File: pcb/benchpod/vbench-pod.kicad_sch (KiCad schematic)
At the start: 116 parts, among them J1 PZ254V-12-22P, SW1 TS-1088-AR02016, SW2 TS-1088-AR02016, U1 ICE40UP5K-SG48ITR, U10 TCAN1044VDRBRQ1, U2 W25Q64JVSSIQ, U24 SN74LVC2G66DCUR, U28 SRV05-4.TCT, U4 ESP32-C3-MINI-1-N4, U5 STM32H563ZGT6, U7 APS6404L-3SQR-ZR, U8 TPS2116DRLR, X1 SX3M48.000B10F20TNN, Y2 6pF ±10ppm SMD2016-4P Crystal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

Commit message: analog v3r2: smaller capacitor packages (same rating and dielectric)
To 0402: 3.3 nF C99 C102 C119 C226 (C26404), 8.2 pF C0G C29 C30 C50 C51
(C1579), 5.1 pF high-Q C207 C208 (C237535; the old C2297586 had 29 in stock).
To 0603: 4.7 uF C2 C3 C5 C220 (C69335), 22 uF C16 C108 C154 C157 (C2762594),
220 nF C189 (C64705), 2.2 uF X7R VCAP C218 C219 (C415535, from 1206).

Kept: C150/C153 (4.7 uF on the ~5 V charge-pump rails, DC-bias derating),
C140 (sees up to 58 V at TVS clamp), all 10 uF and the 22 uF on >5 V rails.
Footprint changes: needs a PCB update. Netlist connectivity unchanged.

Co-Authored-By: Claude Opus 5.5 <noreply@anthropic.com>
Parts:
- C16: footprint Capacitor_SMD:C_0805_2012Metric -> Capacitor_SMD:C_0603_1608Metric; LCSC C45783 -> C2762594; MFR CL21A226MAQNNNE -> CL10A226MO7JZNC
- C2, C220, C3, C5: footprint Capacitor_SMD:C_0805_2012Metric -> Capacitor_SMD:C_0603_1608Metric; LCSC C98192 -> C69335
- C218, C219: footprint Capacitor_SMD:C_1206_3216Metric -> Capacitor_SMD:C_0603_1608Metric; LCSC C50254 -> C415535
- C50, C51: footprint Capacitor_SMD:C_0603_1608Metric -> Capacitor_SMD:C_0402_1005Metric; LCSC C1685 -> C1579
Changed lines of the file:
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@@
 			)
 		)
-		(property "Footprint" "Capacitor_SMD:C_0805_2012Metric"
+		(property "Footprint" "Capacitor_SMD:C_0603_1608Metric"
 			(at 59.9948 129.54 0)
 			(hide yes)
@@
 			)
 		)
-		(property "LCSC" "C98192"
+		(property "LCSC" "C69335"
 			(at 60.96 133.35 0)
 			(hide yes)
@@
 			)
 		)
-		(property "Footprint" "Capacitor_SMD:C_0805_2012Metric"
+		(property "Footprint" "Capacitor_SMD:C_0603_1608Metric"
 			(at 244.8052 36.83 0)
 			(hide yes)
@@
 			)
 		)
-		(property "LCSC" "C98192"
+		(property "LCSC" "C69335"
 			(at 243.84 33.02 0)
 			(hide yes)
@@
 			)
 		)
-		(property "Footprint" "Capacitor_SMD:C_0805_2012Metric"
+		(property "Footprint" "Capacitor_SMD:C_0603_1608Metric"
 			(at 18.0848 162.56 0)
 			(hide yes)
@@
 			)
 		)
-		(property "LCSC" "C98192"
+		(property "LCSC" "C69335"
 			(at 19.05 158.75 0)
 			(hide yes)
@@
 			)
 		)
-		(property "Footprint" "Capacitor_SMD:C_1206_3216Metric"
+		(property "Footprint" "Capacitor_SMD:C_0603_1608Metric"
 			(at 314.6552 236.22 0)
 			(hide yes)
@@
 			)
 		)
-		(property "LCSC" "C50254"
+		(property "LCSC" "C415535"
 			(at 313.69 232.41 0)
 			(hide yes)
@@
 			)
 		)
-		(property "Footprint" "Capacitor_SMD:C_0805_2012Metric"
+		(property "Footprint" "Capacitor_SMD:C_0603_1608Metric"
 			(at 173.6852 34.29 0)
 			(hide yes)
@@
 			)
 		)
-		(property "LCSC" "C45783"
+		(property "LCSC" "C2762594"
 			(at 172.72 30.48 0)
 			(hide yes)
@@
 			)
 		)
-		(property "MFR" "CL21A226MAQNNNE"
+		(property "MFR" "CL10A226MO7JZNC"
 			(at 172.72 30.48 0)
 			(hide yes)
@@
 			)
 		)
-		(property "Footprint" "Capacitor_SMD:C_0603_1608Metric"
+		(property "Footprint" "Capacitor_SMD:C_0402_1005Metric"
 			(at 240.3348 177.8 0)
 			(hide yes)
@@
 			)
 		)
-		(property "LCSC" "C1685"
+		(property "LCSC" "C1579"
 			(at 241.3 173.99 0)
 			(hide yes)
@@
 			)
 		)
-		(property "Footprint" "Capacitor_SMD:C_1206_3216Metric"
+		(property "Footprint" "Capacitor_SMD:C_0603_1608Metric"
 			(at 392.1252 36.83 0)
 			(hide yes)
@@
 			)
 		)
-		(property "LCSC" "C50254"
+		(property "LCSC" "C415535"
 			(at 391.16 33.02 0)
 			(hide yes)
@@
 			)
 		)
-		(property "Footprint" "Capacitor_SMD:C_0603_1608Metric"
+		(property "Footprint" "Capacitor_SMD:C_0402_1005Metric"
 			(at 230.1748 170.18 0)
 			(hide yes)
@@
 			)
 		)
-		(property "LCSC" "C1685"
+		(property "LCSC" "C1579"
 			(at 231.14 166.37 0)
 			(hide yes)
@@
 			)
 		)
-		(property "Footprint" "Capacitor_SMD:C_0805_2012Metric"
+		(property "Footprint" "Capacitor_SMD:C_0603_1608Metric"
 			(at 25.7048 133.35 0)
 			(hide yes)
@@
 			)
 		)
-		(property "LCSC" "C98192"
+		(property "LCSC" "C69335"
 			(at 26.67 129.54 0)
 			(hide yes)

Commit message: analog v3r2: no extra BOM lines from the 0.1 % swaps and cap shrinks
JLC standard assembly charges per unique BOM line, so only keep changes
that replace a whole line:
- Revert 4.7 uF C2 C3 C5 C220 and 22 uF C16 C108 C154 C157 to 0805 (the
  other 4.7 uF/22 uF stay 0805, so the shrink split a line), and 5.1 pF C207
  C208 to the 0603 C2297586 (C140 needs it; 29 in stock = 9 boards).
- Move the remaining 1k (R21 R22 R164 R175), 1.5k (R15) and 2.2k (R58 R62)
  to the same 0.1 % parts as the precision ones, so their old lines go.

BOM: 122 -> 124 unique lines (0.1 % 10k for R109 R110 R111 R123, tantalum
C142). Netlist connectivity unchanged.

Co-Authored-By: Claude Opus 5.5 <noreply@anthropic.com>
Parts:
- C16: footprint Capacitor_SMD:C_0603_1608Metric -> Capacitor_SMD:C_0805_2012Metric; LCSC C2762594 -> C45783; MFR CL10A226MO7JZNC -> CL21A226MAQNNNE
- C2, C220, C3, C5: footprint Capacitor_SMD:C_0603_1608Metric -> Capacitor_SMD:C_0805_2012Metric; LCSC C69335 -> C98192
- R164, R175, R21, R22: LCSC C11702 -> C852624
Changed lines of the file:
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@@
 			)
 		)
-		(property "Footprint" "Capacitor_SMD:C_0603_1608Metric"
+		(property "Footprint" "Capacitor_SMD:C_0805_2012Metric"
 			(at 59.9948 129.54 0)
 			(hide yes)
@@
 			)
 		)
-		(property "LCSC" "C69335"
+		(property "LCSC" "C98192"
 			(at 60.96 133.35 0)
 			(hide yes)
@@
 			)
 		)
-		(property "Footprint" "Capacitor_SMD:C_0603_1608Metric"
+		(property "Footprint" "Capacitor_SMD:C_0805_2012Metric"
 			(at 244.8052 36.83 0)
 			(hide yes)
@@
 			)
 		)
-		(property "LCSC" "C69335"
+		(property "LCSC" "C98192"
 			(at 243.84 33.02 0)
 			(hide yes)
@@
 			)
 		)
-		(property "Footprint" "Capacitor_SMD:C_0603_1608Metric"
+		(property "Footprint" "Capacitor_SMD:C_0805_2012Metric"
 			(at 18.0848 162.56 0)
 			(hide yes)
@@
 			)
 		)
-		(property "LCSC" "C69335"
+		(property "LCSC" "C98192"
 			(at 19.05 158.75 0)
 			(hide yes)
@@
 			)
 		)
-		(property "LCSC" "C11702"
+		(property "LCSC" "C852624"
 			(at 90.17 161.29 90)
 			(hide yes)
@@
 			)
 		)
-		(property "LCSC" "C11702"
+		(property "LCSC" "C852624"
 			(at 259.08 60.96 90)
 			(hide yes)
@@
 			)
 		)
-		(property "Footprint" "Capacitor_SMD:C_0603_1608Metric"
+		(property "Footprint" "Capacitor_SMD:C_0805_2012Metric"
 			(at 173.6852 34.29 0)
 			(hide yes)
@@
 			)
 		)
-		(property "LCSC" "C2762594"
+		(property "LCSC" "C45783"
 			(at 172.72 30.48 0)
 			(hide yes)
@@
 			)
 		)
-		(property "MFR" "CL10A226MO7JZNC"
+		(property "MFR" "CL21A226MAQNNNE"
 			(at 172.72 30.48 0)
 			(hide yes)
@@
 			)
 		)
-		(property "LCSC" "C11702"
+		(property "LCSC" "C852624"
 			(at 288.29 167.64 90)
 			(hide yes)
@@
 			)
 		)
-		(property "Footprint" "Capacitor_SMD:C_0603_1608Metric"
+		(property "Footprint" "Capacitor_SMD:C_0805_2012Metric"
 			(at 25.7048 133.35 0)
 			(hide yes)
@@
 			)
 		)
-		(property "LCSC" "C69335"
+		(property "LCSC" "C98192"
 			(at 26.67 129.54 0)
 			(hide yes)
@@
 			)
 		)
-		(property "LCSC" "C11702"
+		(property "LCSC" "C852624"
 			(at 260.35 87.63 90)
 			(hide yes)

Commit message: analog v3r2: quad DAC (DAC8554) with one channel per output, TMUXes removed
Step A of the analog redesign, relays unchanged:
- U43 DAC8551 -> DAC8554IPWR (C527522, same 24-bit frame family):
  A = TO_3V3, B = TO_5V, C = TO_12V (U51B and the cal2 stage U51C),
  D = DAC_OUTPUT -> U44B -> BUFFER_OUT -> XTR116, so 4-20 mA is now
  independent of the voltage outputs. VREFH = AREF_4V096, VREFL/A0/A1/
  ENABLE/LDAC = GND, IOVDD = +3V3 with new C266 100n (C307331).
- Removed U47 U48 (TMUX1104), U55 (TCA9554 @0x21) with R107 R112 R124,
  C164 C199 C200 C203 C204 C234, and the SDA/SCL sheet pins of this sheet.
- BUFFER_VMID (2.048 V) now goes straight to both +-12 V stages
  (was TO_12V_VMID / TO_ADC_VMID through U48).

Firmware/gateware follow-up (not in this commit): DAC frame control byte
selects the channel (DAC8554: LD1:LD0 = 01, DAC select in DB18:DB17), the
analog path picks a DAC channel instead of U47/U48, and no expander at 0x21.

Checked: pin-to-net diff shows only the intended changes; ERC errors
unchanged (25). BOM 124 -> 123 unique lines. Needs a PCB update.

Co-Authored-By: Claude Opus 5.5 <noreply@anthropic.com>
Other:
- sheet digital to analog v2 ports: added none; removed SCL, SDA
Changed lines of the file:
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@@
 		)
 	)
-	(label "I2C0_SCL"
-		(at 123.19 87.63 0)
-		(effects
-			(font
-				(size 1.27 1.27)
-			)
-			(justify left bottom)
-		)
-	)
 	(label "CAN_TERM_CTRL"
 		(at 185.42 156.21 180)
@@
 		)
 	)
-	(label "I2C0_SDA"
-		(at 123.19 85.09 0)
-		(effects
-			(font
-				(size 1.27 1.27)
-			)
-			(justify left bottom)
-		)
-	)
 	(label "STM32_VDD"
 		(at 373.38 86.36 0)
@@
 			)
 		)
-		(pin "SCL" input
-			(at 123.19 87.63 0)
-			(effects
-				(font
-					(size 1.27 1.27)
-				)
-				(justify right)
-			)
-		)
 		(pin "SCLK" input
 			(at 123.19 78.74 0)
@@
 			)
 		)
-		(pin "SDA" input
-			(at 123.19 85.09 0)
-			(effects
-				(font
-					(size 1.27 1.27)
-				)
-				(justify right)
-			)
-		)
 		(pin "SYNC" input
 			(at 123.19 81.28 0)
@@
 		)
 	)
-	(embedded_fonts no)
 )

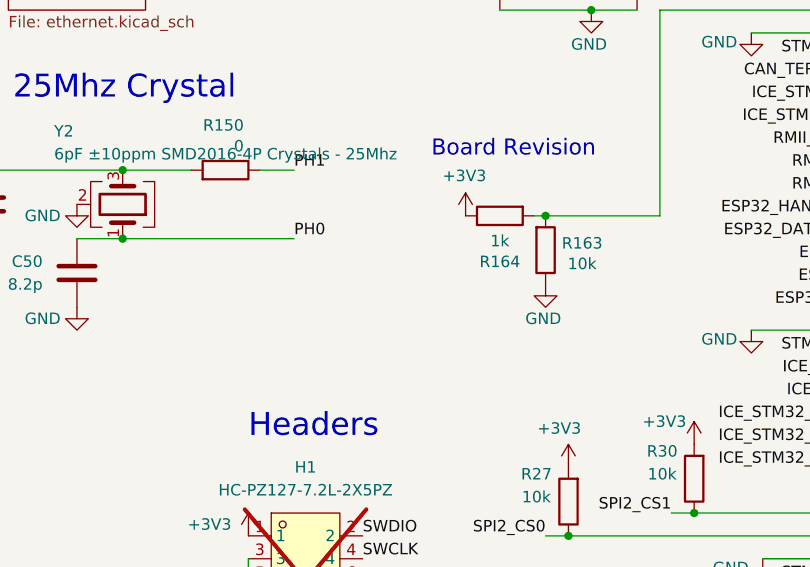
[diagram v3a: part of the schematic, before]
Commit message: analog v3r2: board-rev strap R164 1k -> 2.2k (PA3 2.70 V)
v3 straps PA3 with 1k/10k (3.00 V); v3r2 uses 2.2k/10k (2.70 V) so new
firmware can tell them apart. Still reads HIGH in the pull-down NC test
(~2.59 V loaded), so v2 detection is unchanged, and old firmware runs a
v3r2 board as v3. R164 uses the existing 0.1 % 2.2k line (C326602): no new
BOM line. Note next to the strap documents both values.

Co-Authored-By: Claude Opus 5.5 <noreply@anthropic.com>
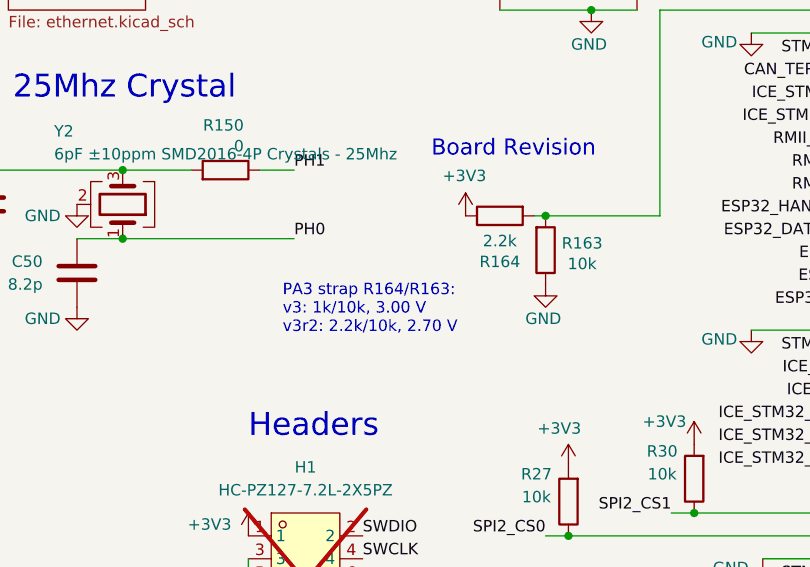
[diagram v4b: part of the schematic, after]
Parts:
- R164: value 1k -> 2.2k; LCSC C852624 -> C326602
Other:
- note added: "PA3 strap R164/R163: v3: 1k/10k, 3.00 V v3r2: 2.2k/10k, 2.70 V"
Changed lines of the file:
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@@
 		)
 	)
+	(text "PA3 strap R164/R163:\nv3: 1k/10k, 3.00 V\nv3r2: 2.2k/10k, 2.70 V"
+		(exclude_from_sim no)
+		(at 264.16 175.26 0)
+		(effects
+			(font
+				(size 1.27 1.27)
+			)
+			(justify left top)
+		)
+	)
 	(text "STM32H563"
 		(exclude_from_sim no)
@@
 			)
 		)
-		(property "Value" "1k"
+		(property "Value" "2.2k"
 			(at 288.29 170.434 90)
 			(show_name no)
@@
 			)
 		)
-		(property "LCSC" "C852624"
+		(property "LCSC" "C326602"
 			(at 288.29 167.64 90)
 			(hide yes)
